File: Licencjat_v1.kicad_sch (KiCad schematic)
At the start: 41 parts, among them J1 Conn_01x02_Socket, J2 Conn_01x02_Socket, J3 Conn_01x01_Socket, J4 Conn_01x01_Socket, J5 Conn_01x01_Socket, J6 Conn_01x01_Socket, Q1 AO3401A, Q2 NPN, Q3 NPN, Q4 NPN, Q5 AO3401A, Q6 AO3401A, Q7 AO3401A, Q8 AO3401A, U1 ATmega328P-A, U2 XC6206PxxxMR, Y1 Crystal_Small

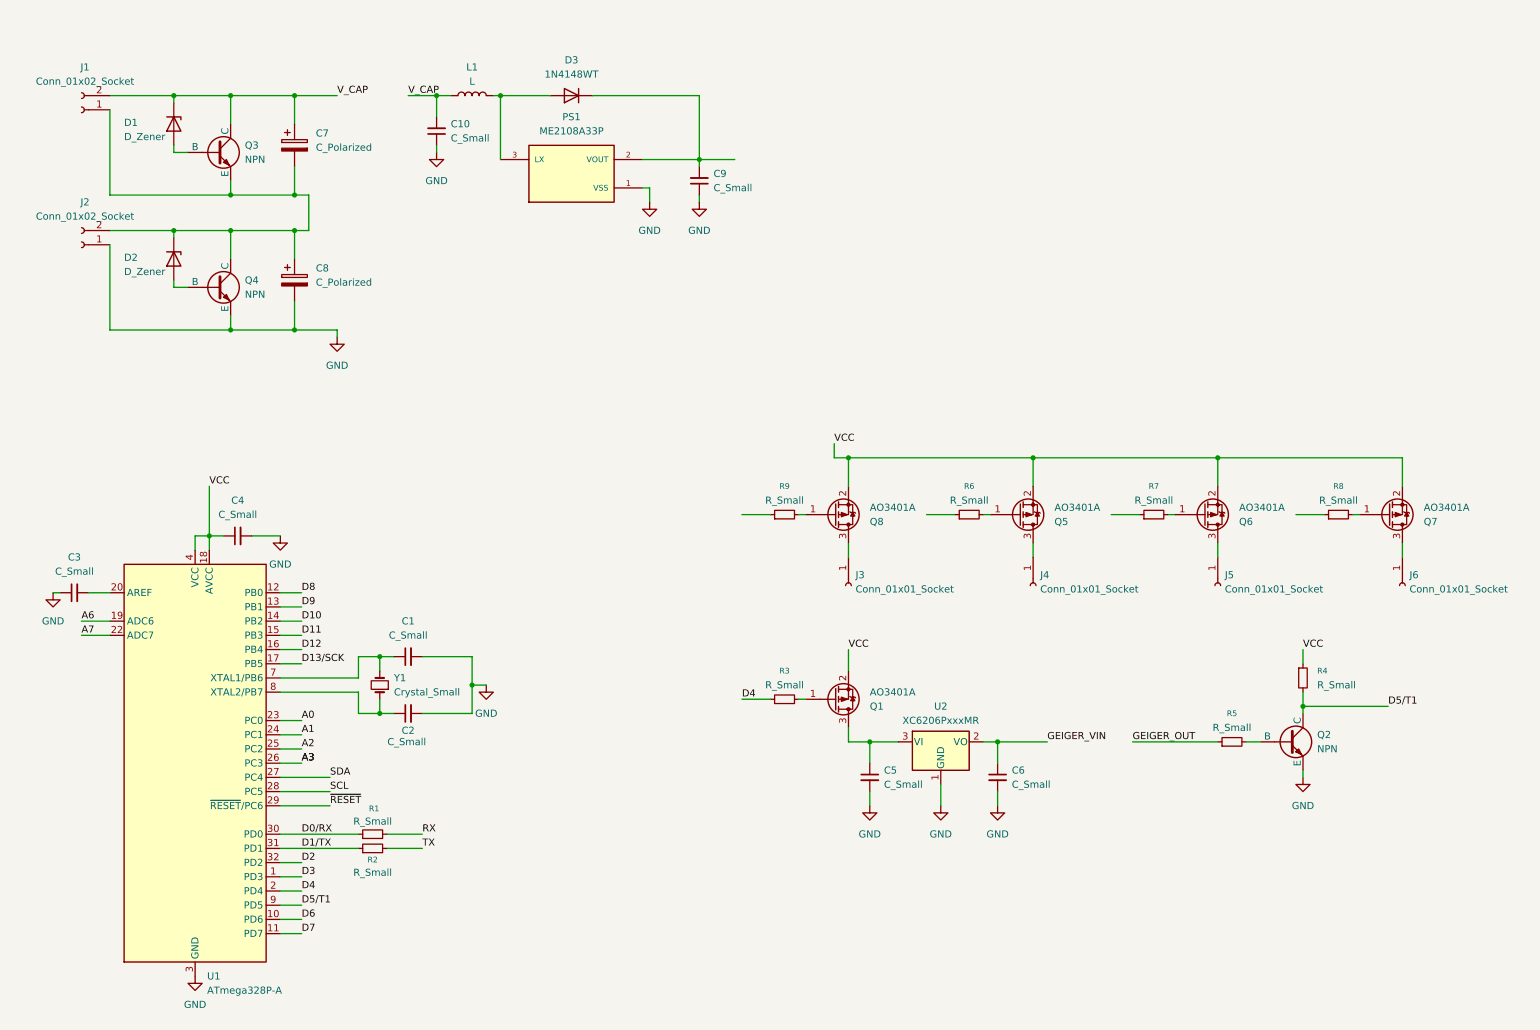
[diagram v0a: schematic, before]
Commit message: Add i2c level shifters
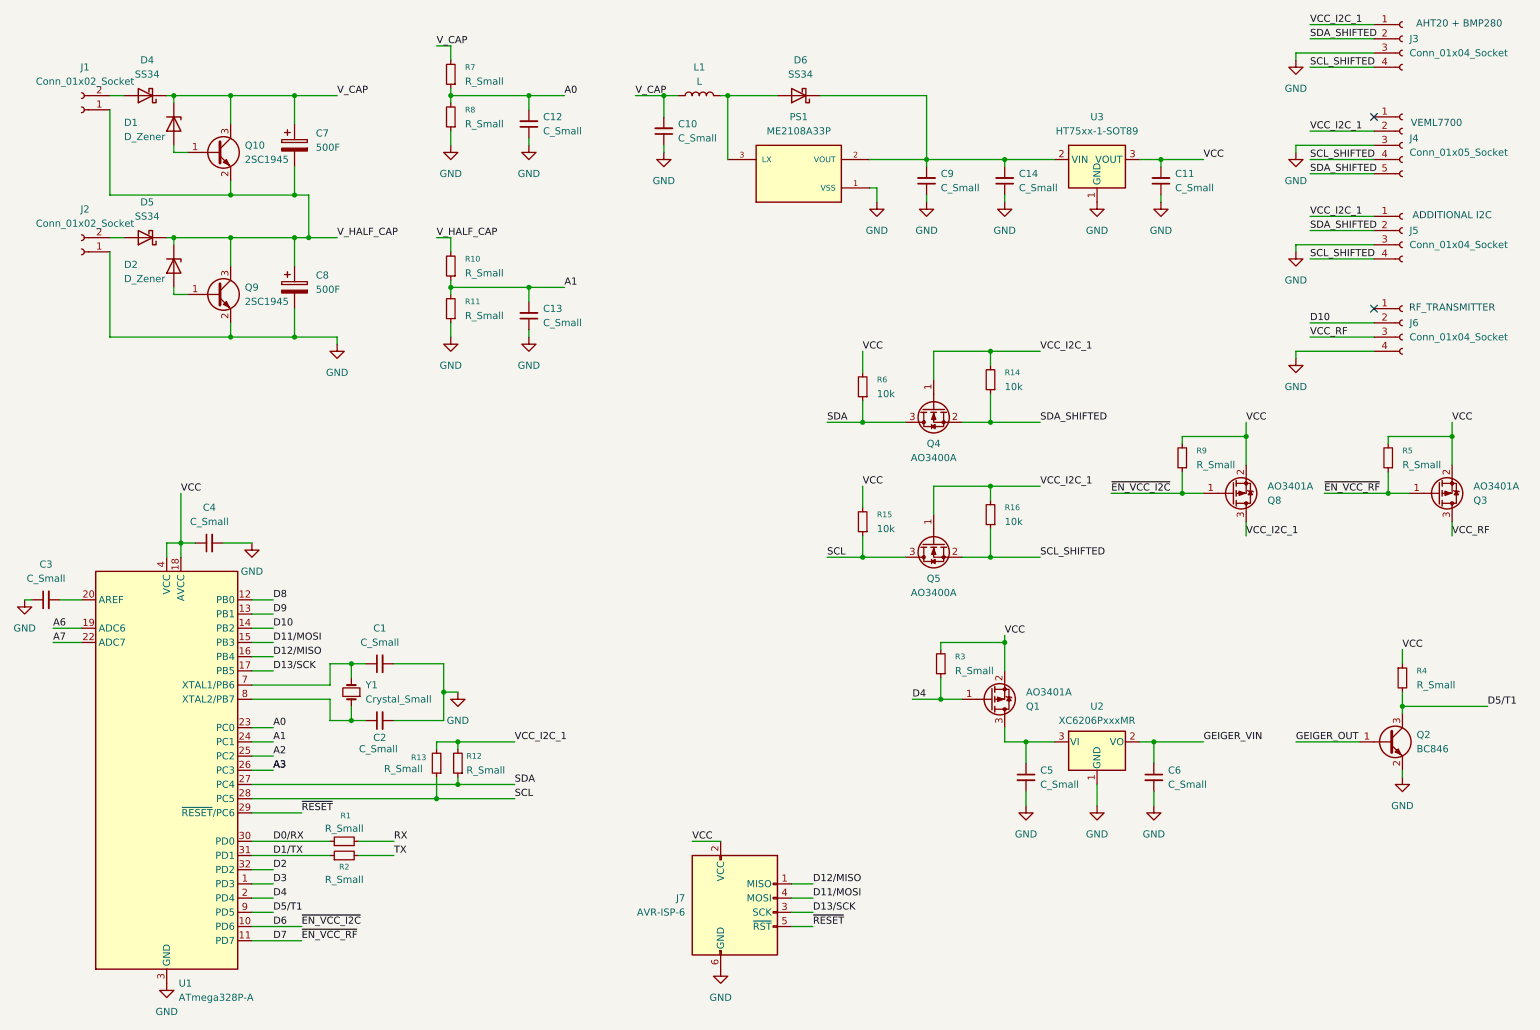
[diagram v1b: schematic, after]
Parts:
- removed D3: 1N4148WT, Diode_SMD:D_SOD-523, symbol Diode:1N4148WT
- removed J3, J4, J5, J6: Conn_01x01_Socket, symbol Connector:Conn_01x01_Socket
- removed Q2, Q3, Q4: NPN, symbol Simulation_SPICE:NPN
- removed Q5, Q6, Q7: AO3401A, Package_TO_SOT_SMD:SOT-23, symbol Transistor_FET:AO3401A
- added C11, C12, C13, C14: C_Small, Capacitor_SMD:C_1206_3216Metric, symbol Device:C_Small
- added D4, D5, D6: SS34, Diode_SMD:D_SMA, symbol Diode:SS34
- added J3: Conn_01x04_Socket, foot_prints:ATH20 + BMP280, symbol Connector:Conn_01x04_Socket
- added J4: Conn_01x05_Socket, foot_prints:VEML7700, symbol Connector:Conn_01x05_Socket
- added J5: Conn_01x04_Socket, Connector_PinHeader_2.54mm:PinHeader_1x04_P2.54mm_Vertical, symbol Connector:Conn_01x04_Socket
- added J6: Conn_01x04_Socket, foot_prints:RF_TRANSMITTER, symbol Connector:Conn_01x04_Socket
- added J7: AVR-ISP-6, Connector_IDC:IDC-Header_2x03_P2.54mm_Vertical, symbol Connector:AVR-ISP-6
- added Q10, Q9: 2SC1945, Package_TO_SOT_THT:TO-220-3_Vertical, symbol Transistor_BJT:2SC1945
- added Q2: BC846, Package_TO_SOT_SMD:SOT-23, symbol Transistor_BJT:BC846
- added Q3: AO3401A, Package_TO_SOT_SMD:SOT-23, symbol Transistor_FET:AO3401A
- added Q4, Q5: AO3400A, Package_TO_SOT_SMD:SOT-23, symbol Transistor_FET:AO3400A
- added R10, R11, R12, R13: R_Small, Resistor_SMD:R_1206_3216Metric, symbol Device:R_Small
- added R14, R15, R16: 10k, Resistor_SMD:R_1206_3216Metric, symbol Device:R_Small
- added U3: HT75xx-1-SOT89, Package_TO_SOT_SMD:SOT-89-3, symbol Regulator_Linear:HT75xx-1-SOT89
- C1, C10, C2, C3, C4, C5, C6, C9: footprint (none) -> Capacitor_SMD:C_1206_3216Metric
- C7, C8: value C_Polarized -> 500F; footprint (none) -> foot_prints:DoubleSolderWirePad_1x01_SMD_2x5mm
- D1, D2: footprint (none) -> Diode_SMD:D_MiniMELF
- J1, J2: footprint (none) -> foot_prints:DoubleSolderWirePad_1x01_SMD_2x5mm
- L1: footprint (none) -> Inductor cd54:IND_CD54_SUM
- R1, R2, R3, R4, R5, R7, R8, R9: footprint (none) -> Resistor_SMD:R_1206_3216Metric
- R6: value R_Small -> 10k; footprint (none) -> Resistor_SMD:R_1206_3216Metric
- Y1: footprint (none) -> Crystal:Crystal_SMD_HC49-SD
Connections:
- net A0: now also R7.1, R8.2, C12.2
- net A1: now also C13.2, R10.1, R11.2
- net D10: now also J6.2 (Pin_2)
- net D13/SCK: now also J7.3 (SCK)
- net D4: now also Q1.1 (G)
- net D5/T1: now also Q2.3 (C)
- net D6: now also Q8.1 (G), R9.1
- net D7: now also R5.1, Q3.1 (G)
- net GEIGER_OUT: now also Q2.1 (B); no longer R5.1
- net GND: now also R8.1, C11.1, C12.1, C13.1, C14.1, J3.3 (Pin_3), J4.3 (Pin_3), J5.3 (Pin_3), J6.4 (Pin_4), J7.6 (GND), Q2.2 (E), Q9.2 (E), R11.1, U3.1 (GND)
- net SCL: now also Q5.3 (D), R13.1, R15.1
- net SDA: now also R6.1, Q4.3 (D), R12.1
- net VCC: now also R3.2, R5.2, R6.2, R9.2, C11.2, J7.2 (VCC), Q3.2 (S), R15.2, U3.3 (VOUT)
- net V_CAP: now also R7.2, D4.1 (K), Q10.3 (C); no longer J1.2 (Pin_2)
- net ~{RESET}: now also J7.5 (~{RST})
- net V_HALF_CAP: now reaches C7.2, C8.1, D2.1 (K), J1.1 (Pin_1)
- net V_HALF_CAP: now also D5.1 (K), Q10.2 (E), Q9.3 (C), R10.2; no longer J2.2 (Pin_2)
- net at D2.2 (A): now also Q9.1 (B)
- net at C9.2, PS1.2 (VOUT): now also C14.2, D6.1 (K), U3.2 (VIN)
- net VCC_I2C_1: now reaches Q8.3 (D)
- net VCC_I2C_1: now also J3.1 (Pin_1), J4.2 (Pin_2), J5.1 (Pin_1), Q4.1 (G), Q5.1 (G), R12.2, R13.2, R14.2, R16.2
- net at D1.2 (A): now also Q10.1 (B)
- net at L1.2, PS1.3 (LX): now also D6.2 (A)
- net D11 renamed D11/MOSI
- net D11/MOSI: now also J7.4 (MOSI)
- net D12 renamed D12/MISO
- net D12/MISO: now also J7.1 (MISO)
- new net: D4.2 (A), J1.2 (Pin_2)
- new net: D5.2 (A), J2.2 (Pin_2)
- new net SCL_SHIFTED: J3.4 (Pin_4), J4.4 (Pin_4), J5.4 (Pin_4), Q5.2 (S), R16.1
- new net SDA_SHIFTED: J3.2 (Pin_2), J4.5 (Pin_5), J5.2 (Pin_2), Q4.2 (S), R14.1
- new net VCC_RF: J6.3 (Pin_3), Q3.3 (D)
- no-connect marks 0 -> 2
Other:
- note added: "ADDITIONAL I2C"
- note added: "AHT20 + BMP280"
- note added: "RF_TRANSMITTER"
- note added: "VEML7700"
- moved on the sheet: C1, C10, C2, C3, C4, C5, C6, C8, C9, D2, J2, L1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

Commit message: Set pull-up resistors to 10k
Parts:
- R12, R13, R3, R4, R5, R9: value R_Small -> 10k
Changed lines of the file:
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@@
 			)
 		)
-		(property "Value" "R_Small"
+		(property "Value" "10k"
 			(at 95.504 151.13 0)
 			(effects
@@
 			)
 		)
-		(property "Value" "R_Small"
+		(property "Value" "10k"
 			(at 182.88 133.3499 0)
 			(effects
@@
 			)
 		)
-		(property "Value" "R_Small"
+		(property "Value" "10k"
 			(at 226.06 96.5199 0)
 			(effects
@@
 			)
 		)
-		(property "Value" "R_Small"
+		(property "Value" "10k"
 			(at 262.89 96.5199 0)
 			(effects
@@
 			)
 		)
-		(property "Value" "R_Small"
+		(property "Value" "10k"
 			(at 265.43 135.8899 0)
 			(effects
@@
 			)
 		)
-		(property "Value" "R_Small"
-			(at 80.772 150.876 0)
+		(property "Value" "10k"
+			(at 85.344 151.13 0)
 			(effects
 				(font

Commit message: Add 1Wire, RF Level SHifter and better footprints
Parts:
- added J8: GEIGER, Connector_PinHeader_2.54mm:PinHeader_1x03_P2.54mm_Vertical, symbol Connector:Conn_01x03_Socket
- added J9: 1_WIRE, Connector_PinHeader_2.54mm:PinHeader_1x03_P2.54mm_Vertical, symbol Connector:Conn_01x03_Socket
- added Q11, Q6: AO3400A, Package_TO_SOT_SMD:SOT-23, symbol Transistor_FET:AO3400A
- added Q7: AO3401A, Package_TO_SOT_SMD:SOT-23, symbol Transistor_FET:AO3401A
- added R17: 47k, Resistor_SMD:R_1206_3216Metric, symbol Device:R_Small
- added R18, R19, R20, R21, R22: 10k, Resistor_SMD:R_1206_3216Metric, symbol Device:R_Small
- C10, C11, C5, C6, C9: value C_Small -> 10u
- C12, C13: value C_Small -> 100n
- C14: value C_Small -> 1u
- C7, C8: footprint foot_prints:DoubleSolderWirePad_1x01_SMD_2x5mm -> Project Elements:Super Capacitor
- J3: value Conn_01x04_Socket -> AHT20 + BMP280
- J4: value Conn_01x05_Socket -> VEML7700
- J5: value Conn_01x04_Socket -> ADDITIONAL I2C
- J6: value Conn_01x04_Socket -> RF_TRANSMITTER
- Q10, Q9: footprint Package_TO_SOT_THT:TO-220-3_Vertical -> Project Elements:TO-220-3_Vertical+Radiator
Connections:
- net D10: now also Q11.3 (D), R21.1; no longer J6.2 (Pin_2)
- net D5/T1: now also C14.1, R17.1; no longer Q2.3 (C), R4.2
- net SCL_SHIFTED: now also J5.3 (Pin_3); no longer J5.4 (Pin_4)
- net VCC: now also Q7.2 (S), R18.2, R20.2, R21.2
- net VCC_I2C_1: no longer J3.1 (Pin_1), Q4.1 (G), Q5.1 (G), R12.2, R13.2, R14.2, R16.2
- net VCC_RF: now also Q11.1 (G), R22.2
- net at C9.2, D6.1 (K), PS1.2 (VOUT)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: no longer C14.2
- net GEIGER_OUT renamed GEIGER_IN
- net GEIGER_IN: now also J8.2 (Pin_2)
- net GEIGER_VIN renamed VCC_GEIGER
- net VCC_GEIGER: now also J8.1 (Pin_1)
- removed net GND: C1.2, C10.1, C11.1, C12.1, C13.1, C14.1, C2.2, C3.1, C4.2, C5.2, C6.2, C8.2, C9.1, J2.1 (Pin_1), J3.3 (Pin_3), J4.3 (Pin_3), J5.3 (Pin_3), J6.4 (Pin_4), J7.6 (GND), PS1.1 (VSS), Q2.2 (E), Q9.2 (E), R11.1, R8.1, U1.21 (GND), U1.3 (GND), U1.5 (GND), U2.1 (GND), U3.1 (GND)
- new net: Q2.3 (C), R17.2, R4.2
- new net: C1.2, C2.2
- new net: U1.21 (GND), U1.3 (GND), U1.5 (GND)
- new net: C8.2, J2.1 (Pin_1), Q9.2 (E)
- new net 1_WIRE: Q6.3 (D), R18.1
- new net 1_WIRE_SHIFTED: J9.2 (Pin_2), Q6.2 (S), R19.1
- new net RF_DATA_SHIFTED: J6.2 (Pin_2), Q11.2 (S), R22.1
- new net VCC_1_WIRE: J9.1 (Pin_1), Q6.1 (G), Q7.3 (D), R19.2
- new net VCC_I2C: J3.1 (Pin_1), Q4.1 (G), Q5.1 (G), R12.2, R13.2, R14.2, R16.2
- new net ~{EN_VCC_1_WIRE}: Q7.1 (G), R20.1
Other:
- note removed: "ADDITIONAL I2C"
- note removed: "AHT20 + BMP280"
- note removed: "RF_TRANSMITTER"
- note removed: "VEML7700"
- moved on the sheet: C1, C11, C12, C2, C3, C4, C5, C6, C9, J3, J4, J5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

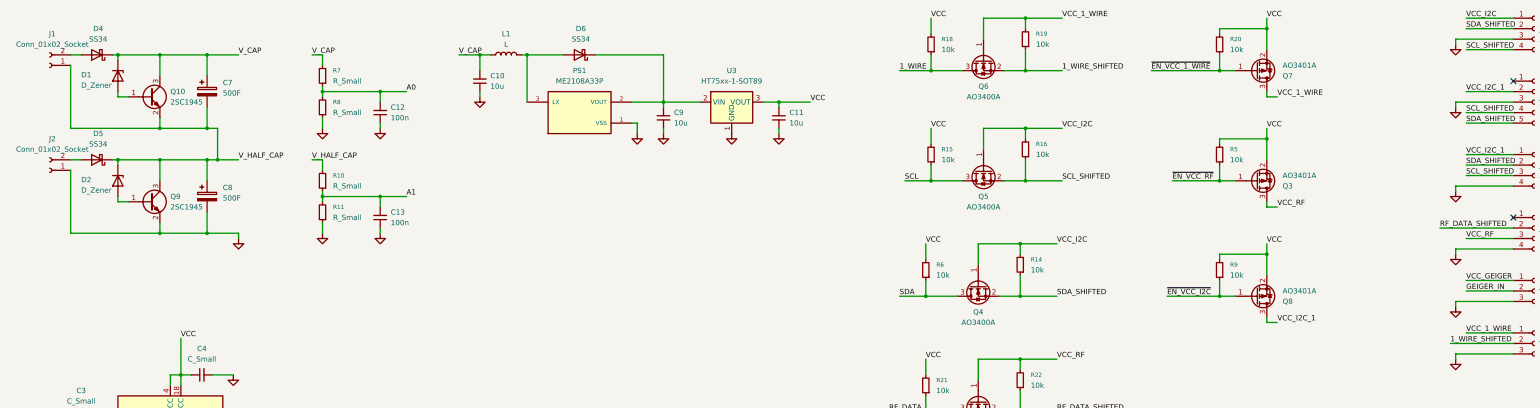
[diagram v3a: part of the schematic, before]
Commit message: Start placing components
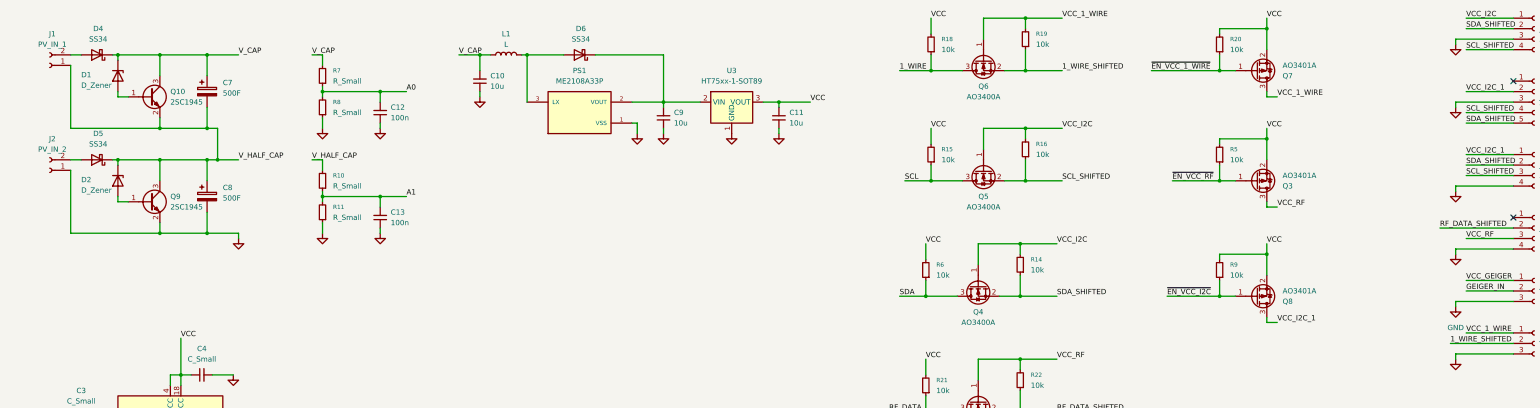
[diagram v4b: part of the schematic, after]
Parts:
- J1: value Conn_01x02_Socket -> PV_IN_1; footprint foot_prints:DoubleSolderWirePad_1x01_SMD_2x5mm -> Connector_PinHeader_2.54mm:PinHeader_1x02_P2.54mm_Vertical
- J2: value Conn_01x02_Socket -> PV_IN_2; footprint foot_prints:DoubleSolderWirePad_1x01_SMD_2x5mm -> Connector_PinHeader_2.54mm:PinHeader_1x02_P2.54mm_Vertical
- J3: footprint foot_prints:ATH20 + BMP280 -> Project Modules:ATH20 + BMP280
- J4: footprint foot_prints:VEML7700 -> Project Modules:VEML7700
- J6: footprint foot_prints:RF_TRANSMITTER -> Project Modules:RF_TRANSMITTER
- L1: footprint Inductor cd54:IND_CD54_SUM -> CD54:IND_CD54_SUM
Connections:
- net GND: now reaches C9.1
- net GND: now also C1.2, C10.1, C11.1, C13.1, C14.2, C2.2, C3.1, C4.2, C5.2, C6.2, C8.2, J2.1 (Pin_1), J3.3 (Pin_3), J4.3 (Pin_3), J5.4 (Pin_4), J6.4 (Pin_4), J7.6 (GND), J8.3 (Pin_3), J9.3 (Pin_3), PS1.1 (VSS), Q2.2 (E), Q9.2 (E), R11.1, U1.21 (GND), U1.3 (GND), U1.5 (GND), U2.1 (GND), U3.1 (GND)
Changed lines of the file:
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@@
 			)
 		)
-		(property "Value" "~"
+		(property "Value" "GND"
 			(at 306.07 167.64 0)
 			(effects
@@
 					(size 1.27 1.27)
 				)
+				(hide yes)
 			)
 		)
@@
 			)
 		)
-		(property "Value" "~"
+		(property "Value" "GND"
 			(at 318.77 167.64 0)
 			(effects
@@
 					(size 1.27 1.27)
 				)
+				(hide yes)
 			)
 		)
@@
 			)
 		)
-		(property "Value" "~"
+		(property "Value" "GND"
 			(at 175.26 54.61 0)
 			(effects
@@
 					(size 1.27 1.27)
 				)
+				(hide yes)
 			)
 		)
@@
 			)
 		)
-		(property "Value" "~"
+		(property "Value" "GND"
 			(at 367.03 33.02 0)
 			(effects
@@
 					(size 1.27 1.27)
 				)
+				(hide yes)
 			)
 		)
@@
 			)
 		)
-		(property "Value" "~"
+		(property "Value" "GND"
 			(at 30.48 123.19 0)
 			(effects
@@
 					(size 1.27 1.27)
 				)
+				(hide yes)
 			)
 		)
@@
 			)
 		)
-		(property "Value" "~"
+		(property "Value" "GND"
 			(at 367.03 48.26 0)
 			(effects
@@
 			)
 		)
-		(property "Value" "~"
+		(property "Value" "GND"
 			(at 106.68 78.74 0)
 			(effects
@@
 					(size 1.27 1.27)
 				)
+				(hide yes)
 			)
 		)
@@
 			)
 		)
-		(property "Value" "~"
+		(property "Value" "GND"
 			(at 191.77 54.61 0)
 			(effects
@@
 					(size 1.27 1.27)
 				)
+				(hide yes)
 			)
 		)
@@
 			)
 		)
-		(property "Value" "Conn_01x02_Socket"
+		(property "Value" "PV_IN_1"
 			(at 27.305 27.94 0)
 			(effects
@@
 			)
 		)
-		(property "Footprint" "foot_prints:DoubleSolderWirePad_1x01_SMD_2x5mm"
+		(property "Footprint" "Connector_PinHeader_2.54mm:PinHeader_1x02_P2.54mm_Vertical"
 			(at 26.67 33.02 0)
 			(effects
@@
 			)
 		)
-		(property "Value" "~"
+		(property "Value" "GND"
 			(at 328.93 167.64 0)
 			(effects
@@
 					(size 1.27 1.27)
 				)
+				(hide yes)
 			)
 		)
@@
 			)
 		)
-		(property "Footprint" "foot_prints:ATH20 + BMP280"
+		(property "Footprint" "Project Modules:ATH20 + BMP280"
 			(at 386.08 24.13 0)
 			(effects
@@
 	)
 	(symbol
+		(lib_name "GND_1")
 		(lib_id "power:GND")
 		(at 168.91 49.53 0)
@@
 			)
 		)
-		(property "Value" "~"
+		(property "Value" "GND"
 			(at 168.91 54.61 0)
 			(effects
@@
 					(size 1.27 1.27)
 				)
+				(hide yes)
 			)
 		)
@@
 			)
 		)
-		(property "Value" "~"
+		(property "Value" "GND"
 			(at 92.71 78.74 0)
 			(effects
@@
 					(size 1.27 1.27)
 				)
+				(hide yes)
 			)
 		)
@@
 			)
 		)
-		(property "Value" "~"
+		(property "Value" "GND"
 			(at 265.43 167.64 0)
 			(effects
@@
 					(size 1.27 1.27)
 				)
+				(hide yes)
 			)
 		)
@@
 			)
 		)
-		(property "Value" "~"
+		(property "Value" "GND"
 			(at 55.88 191.77 0)
 			(effects
@@
 					(size 1.27 1.27)
 				)
+				(hide yes)
 			)
 		)
@@
 			)
 		)
-		(property "Value" "~"
+		(property "Value" "GND"
 			(at 130.81 45.72 0)
 			(effects
@@
 					(size 1.27 1.27)
 				)
+				(hide yes)
 			)
 		)
@@
 			)
 		)
-		(property "Value" "~"
+		(property "Value" "GND"
 			(at 252.73 167.64 0)
 			(effects
@@
 					(size 1.27 1.27)
 				)
+				(hide yes)
 			)
 		)
@@
 			)
 		)
-		(property "Value" "~"
+		(property "Value" "GND"
 			(at 49.53 241.3 0)
 			(effects
@@
 					(size 1.27 1.27)
 				)
+				(hide yes)
 			)
 		)
@@
 			)
 		)
-		(property "Value" "~"
+		(property "Value" "GND"
 			(at 71.12 113.03 0)
 			(effects
@@
 					(size 1.27 1.27)
 				)
+				(hide yes)
 			)
 		)
@@
 			)
 		)
-		(property "Value" "~"
+		(property "Value" "GND"
 			(at 107.95 139.7 0)
 			(effects
@@
 					(size 1.27 1.27)
 				)
+				(hide yes)
 			)
 		)
@@
 			)
 		)
-		(property "Value" "~"
+		(property "Value" "GND"
 			(at 367.03 68.58 0)
 			(effects
@@
 			)
 		)
-		(property "Value" "~"
+		(property "Value" "GND"
 			(at 367.03 96.52 0)
 			(effects
@@
 			)
 		)
-		(property "Value" "~"
+		(property "Value" "GND"
 			(at 367.03 83.82 0)
 			(effects
@@
 					(size 1.27 1.27)
 				)
+				(hide yes)
 			)
 		)
@@
 			)
 		)
-		(property "Value" "~"
+		(property "Value" "GND"
 			(at 72.39 80.01 0)
 			(effects
@@
 					(size 1.27 1.27)
 				)
+				(hide yes)
 			)
 		)
@@
 			)
 		)
-		(property "Footprint" "Inductor cd54:IND_CD54_SUM"
+		(property "Footprint" "CD54:IND_CD54_SUM"
 			(at 137.16 30.48 0)
 			(effects
@@
 			)
 		)
-		(property "Value" "Conn_01x02_Socket"
+		(property "Value" "PV_IN_2"
 			(at 27.305 53.34 0)
 			(effects
@@
 			)
 		)
-		(property "Footprint" "foot_prints:DoubleSolderWirePad_1x01_SMD_2x5mm"
+		(property "Footprint" "Connector_PinHeader_2.54mm:PinHeader_1x02_P2.54mm_Vertical"
 			(at 26.67 58.42 0)
 			(effects
@@
 			)
 		)
-		(property "Footprint" "foot_prints:VEML7700"
+		(property "Footprint" "Project Modules:VEML7700"
 			(at 386.08 41.91 0)
 			(effects
@@
 			)
 		)
-		(property "Footprint" "foot_prints:RF_TRANSMITTER"
+		(property "Footprint" "Project Modules:RF_TRANSMITTER"
 			(at 386.08 72.39 0)
 			(effects
@@
 			)
 		)
-		(property "Value" "~"
+		(property "Value" "GND"
 			(at 367.03 109.22 0)
 			(effects
@@
 					(size 1.27 1.27)
 				)
+				(hide yes)
 			)
 		)
@@
 			)
 		)
-		(property "Value" "~"
+		(property "Value" "GND"
 			(at 203.2 54.61 0)
 			(effects
@@
 					(size 1.27 1.27)
 				)
+				(hide yes)
 			)
 		)
